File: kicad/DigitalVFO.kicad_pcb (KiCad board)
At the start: 2 copper layers, 99.6 x 49.8 mm, 46 parts, among them J1 RF Out, J2 Battery, J3 SW_LED, Q1 2N2222A, SW1 Rotary_Encoder, U1 74HC14, U2 Teensy3.2, U3 LCD1602A, U4 DDS-60

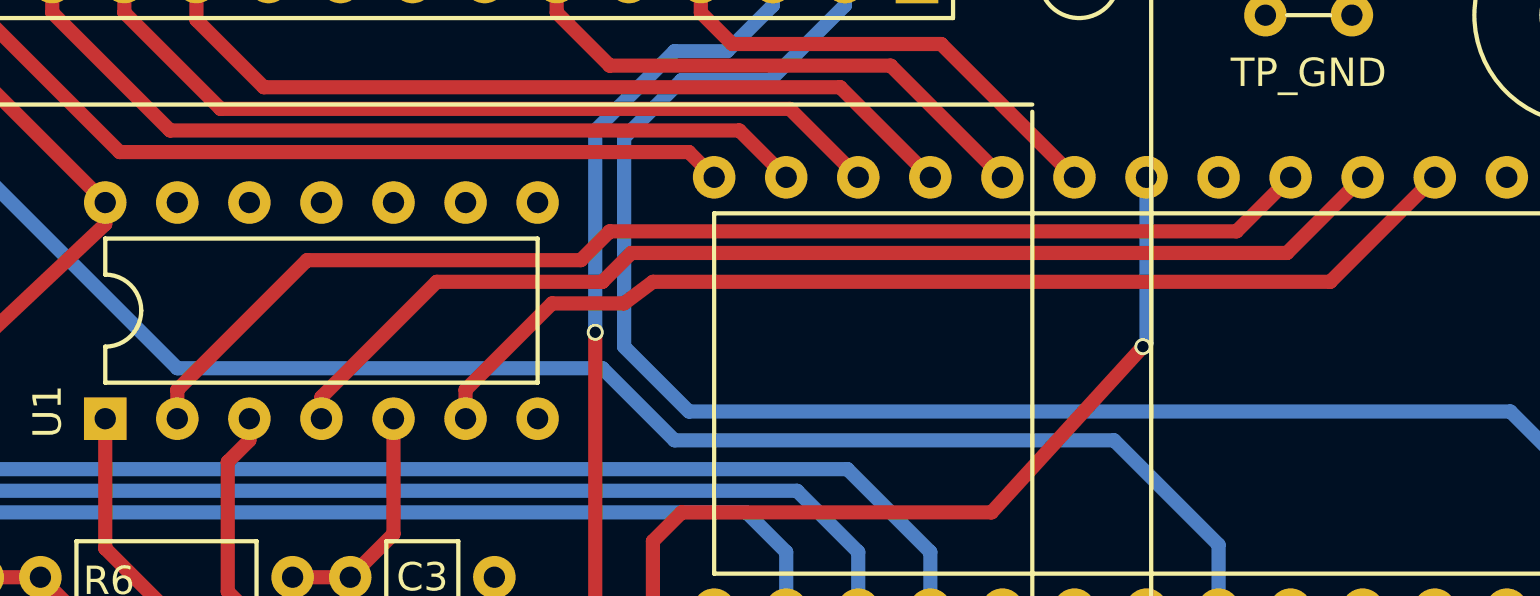
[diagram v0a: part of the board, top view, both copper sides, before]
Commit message: Better track layout
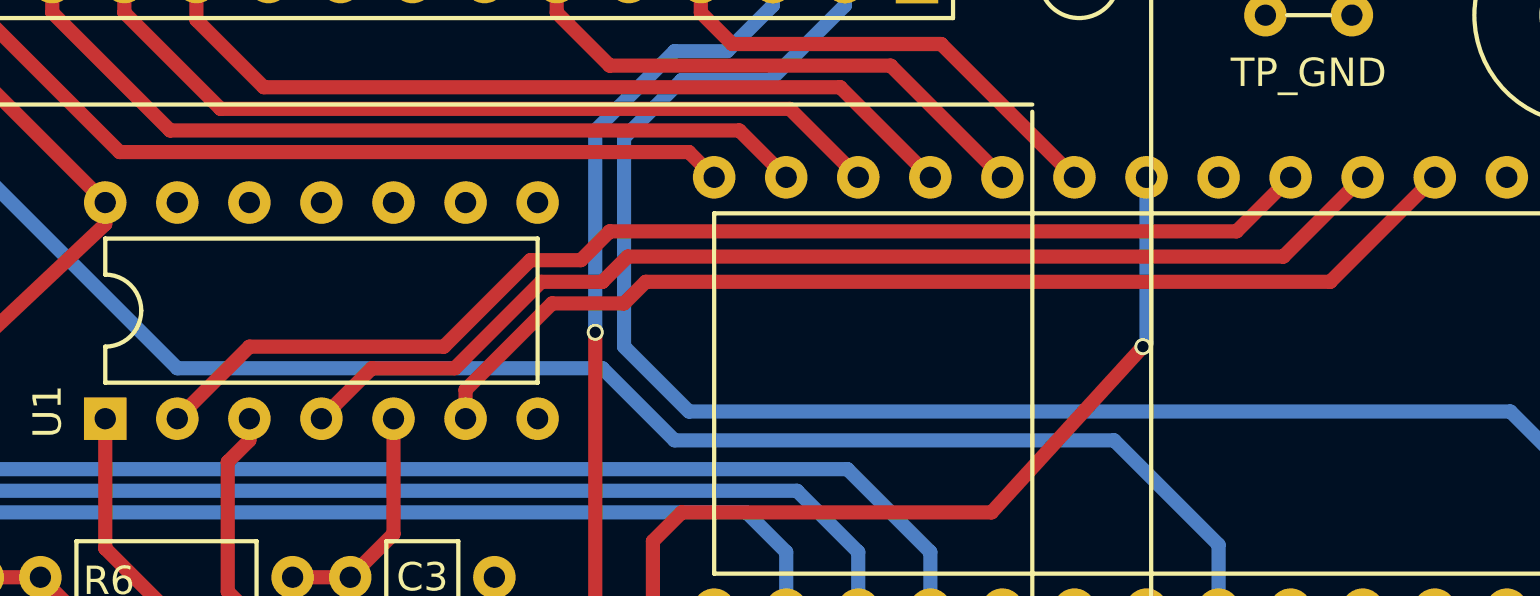
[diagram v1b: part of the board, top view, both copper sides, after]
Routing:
- net Net-(U1-Pad2): track 43.4 -> 42.8 mm

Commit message: Added back silkscreen for test points
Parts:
- moved TP_BATT 0.28 mm to (135.9, 118.5)
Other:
- board text added: "Batt"
- board text added: "LED"
- board text added: "RE"
- board text added: "TP_+5V"
- board text added: "TP_BATT"
- board text added: "TP_BMON"
- board text added: "TP_GND"
- board text added: "TP_RF"
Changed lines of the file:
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@@
     (area 105.515999 69.129 241.605481 126.513001)
     (thickness 1.6)
-    (drawings 7)
+    (drawings 16)
     (tracks 188)
     (zones 0)
@@
     (visible_elements FFFFFF7F)
     (pcbplotparams
-      (layerselection 0x00000_80000001)
+      (layerselection 0x00030_80000001)
       (usegerberextensions false)
       (excludeedgelayer true)
@@
   )
   (module DigitalVFO:TestPoint (layer F.Cu)
-    (at 136.144 118.618)
-    (fp_text reference TP_BATT (at 0 -1.778) (layer F.SilkS)
+    (at 135.89 118.491)
+    (fp_text reference TP_BATT (at 0 -2.159) (layer F.SilkS)
       (effects (font (size 1 1) (thickness 0.15)))
     )
@@
     (pad "" np_thru_hole circle (at 0 0) (size 3 3) (drill 3) (layers *.Cu *.Mask)
       (solder_mask_margin 2.5) (zone_connect 0))
+  )
+  (gr_text LED (at 175.133 115.443) (layer F.SilkS)
+    (effects (font (size 1 1) (thickness 0.2)))
+  )
+  (gr_text RE (at 161.925 115.443) (layer F.SilkS)
+    (effects (font (size 1 1) (thickness 0.2)))
+  )
+  (gr_text Batt (at 152.781 115.443) (layer F.SilkS)
+    (effects (font (size 1 1) (thickness 0.2)))
+  )
+  (gr_text TP_GND (at 180.594 117.602) (layer B.SilkS)
+    (effects (font (size 1 1) (thickness 0.25)) (justify mirror))
+  )
+  (gr_text TP_BATT (at 135.89 116.332) (layer B.SilkS)
+    (effects (font (size 1 1) (thickness 0.25)) (justify mirror))
+  )
+  (gr_text TP_+5V (at 216.408 104.648) (layer B.SilkS)
+    (effects (font (size 1 1) (thickness 0.25)) (justify mirror))
+  )
+  (gr_text TP_RF (at 195.707 117.094) (layer B.SilkS)
+    (effects (font (size 1 1) (thickness 0.25)) (justify mirror))
+  )
+  (gr_text TP_BMON (at 204.978 102.108) (layer B.SilkS)
+    (effects (font (size 1 1) (thickness 0.25)) (justify mirror))
+  )
+  (gr_text TP_GND (at 207.137 77.343) (layer B.SilkS)
+    (effects (font (size 1 1) (thickness 0.25)) (justify mirror))
   )
   (gr_line (start 121.412 121.158) (end 121.412 71.374) (angle 90) (layer Edge.Cuts) (width 0.15))
@@
   (segment (start 203.835 93.853) (end 203.835 96.139) (width 0.5) (layer B.Cu) (net 15))
   (segment (start 200.152 90.17) (end 203.835 93.853) (width 0.5) (layer B.Cu) (net 15))
-  (segment (start 184.658 90.17) (end 200.152 90.17) (width 0.5) (layer B.Cu) (net 15))
-  (segment (start 182.118 87.63) (end 184.658 90.17) (width 0.5) (layer B.Cu) (net 15))
-  (segment (start 167.132 87.63) (end 182.118 87.63) (width 0.5) (layer B.Cu) (net 15))
-  (segment (start 160.02 80.518) (end 167.132 87.63) (width 0.5) (layer B.Cu) (net 15))
+  (segment (start 183.388 90.17) (end 200.152 90.17) (width 0.5) (layer B.Cu) (net 15))
+  (segment (start 177.673 84.455) (end 183.388 90.17) (width 0.5) (layer B.Cu) (net 15))
+  (segment (start 163.957 84.455) (end 177.673 84.455) (width 0.5) (layer B.Cu) (net 15))
+  (segment (start 160.02 80.518) (end 163.957 84.455) (width 0.5) (layer B.Cu) (net 15))
   (segment (start 183.896 97.79) (end 183.896 93.726) (width 0.5) (layer F.Cu) (net 16))
   (segment (start 184.912 92.71) (end 195.834 92.71) (width 0.5) (layer F.Cu) (net 16))
@@
   (segment (start 204.47 118.872) (end 209.62874 113.71326) (width 0.5) (layer F.Cu) (net 34))
   (segment (start 209.62874 113.71326) (end 209.62874 113.284) (width 0.5) (layer F.Cu) (net 34))
-  (segment (start 137.668 118.618) (end 134.62 118.618) (width 0.5) (layer B.Cu) (net 35))
-  (segment (start 142.24 110.236) (end 142.24 114.046) (width 0.5) (layer B.Cu) (net 35))
-  (segment (start 142.24 114.046) (end 137.668 118.618) (width 0.5) (layer B.Cu) (net 35))
+  (segment (start 142.24 110.236) (end 142.24 113.665) (width 0.5) (layer B.Cu) (net 35) (status 400000))
+  (segment (start 142.24 113.665) (end 137.414 118.491) (width 0.5) (layer B.Cu) (net 35) (status 800000))
+  (segment (start 137.414 118.491) (end 134.366 118.491) (width 0.5) (layer B.Cu) (net 35) (status C00000))
   (segment (start 148.336 103.378) (end 148.336 105.156) (width 0.5) (layer F.Cu) (net 35))
   (segment (start 148.336 105.156) (end 145.034 108.458) (width 0.5) (layer F.Cu) (net 35))

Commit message: Updated the PCB
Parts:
- removed the REF** at (199.1, 105.0)
- removed the REF** at (123.7, 105.0)
